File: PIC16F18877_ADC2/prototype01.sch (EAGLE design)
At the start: 34 parts, among them CN1 12V_IN, CN3 UART_IF, CN4 PIC_CN_H, CN5 AE-MICRO-SD-DIP, CN6 I2C_IF, SW1 10-XX, U1 XC6202P332TH, U2 PIC16F18877-I/P, U3 AE-AQM1602A, U4 AE-RTC-8564NB

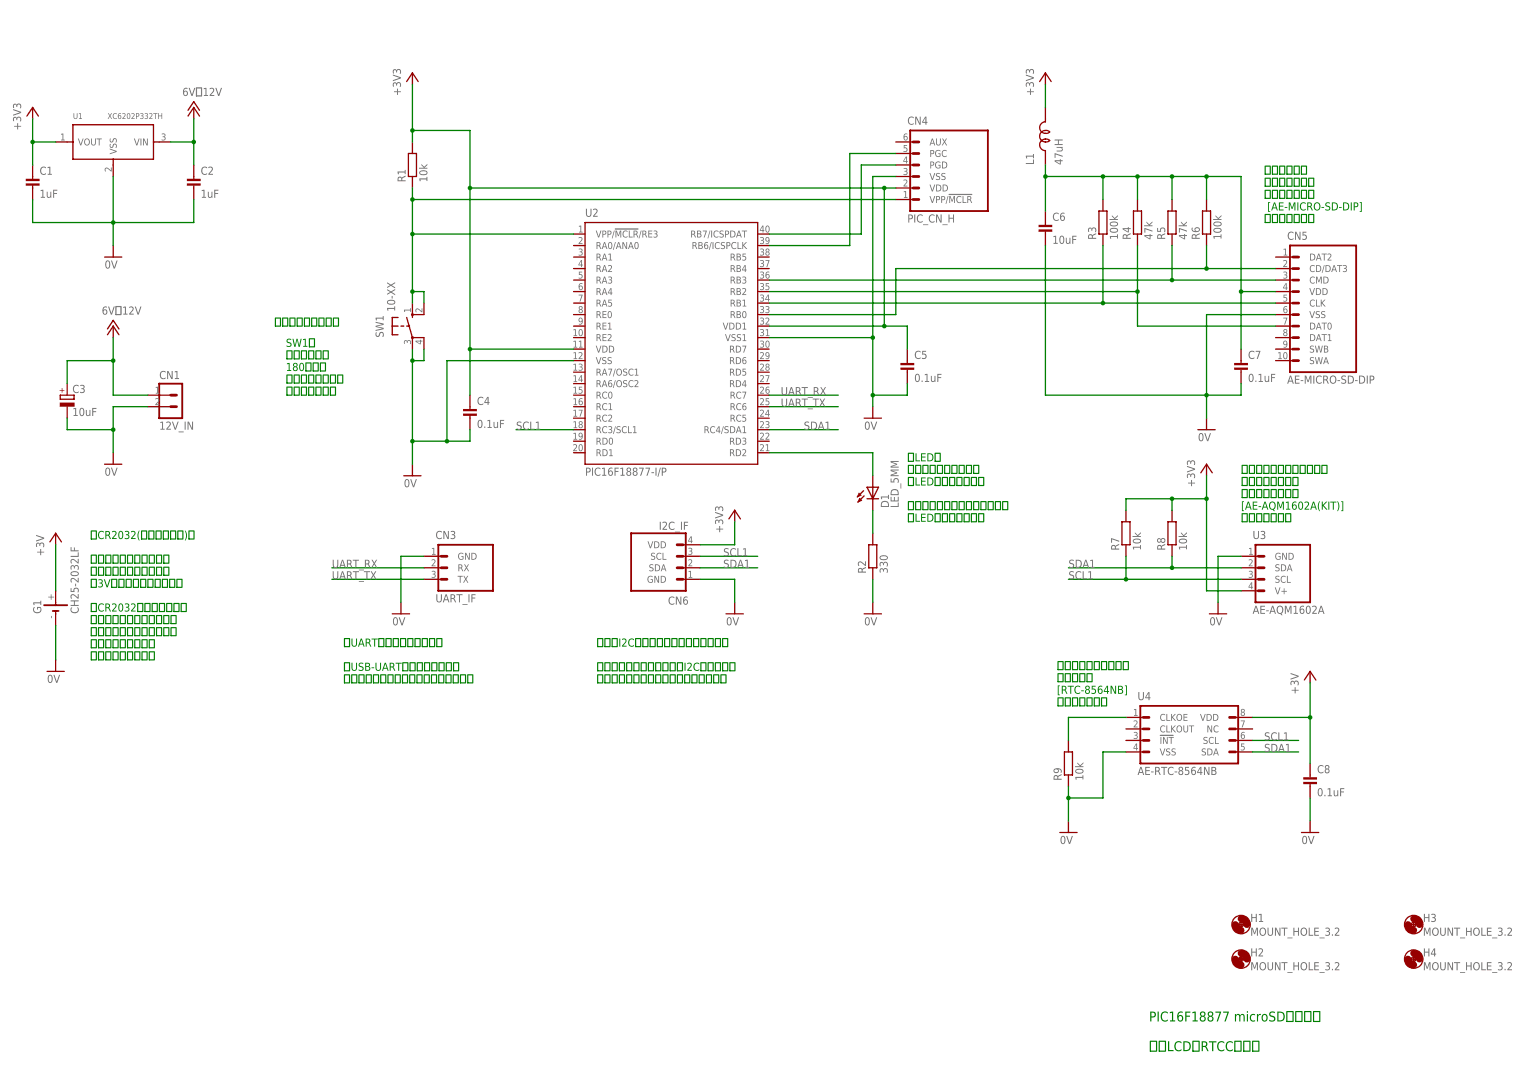
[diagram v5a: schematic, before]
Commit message: GPIO接続用コネクター増設
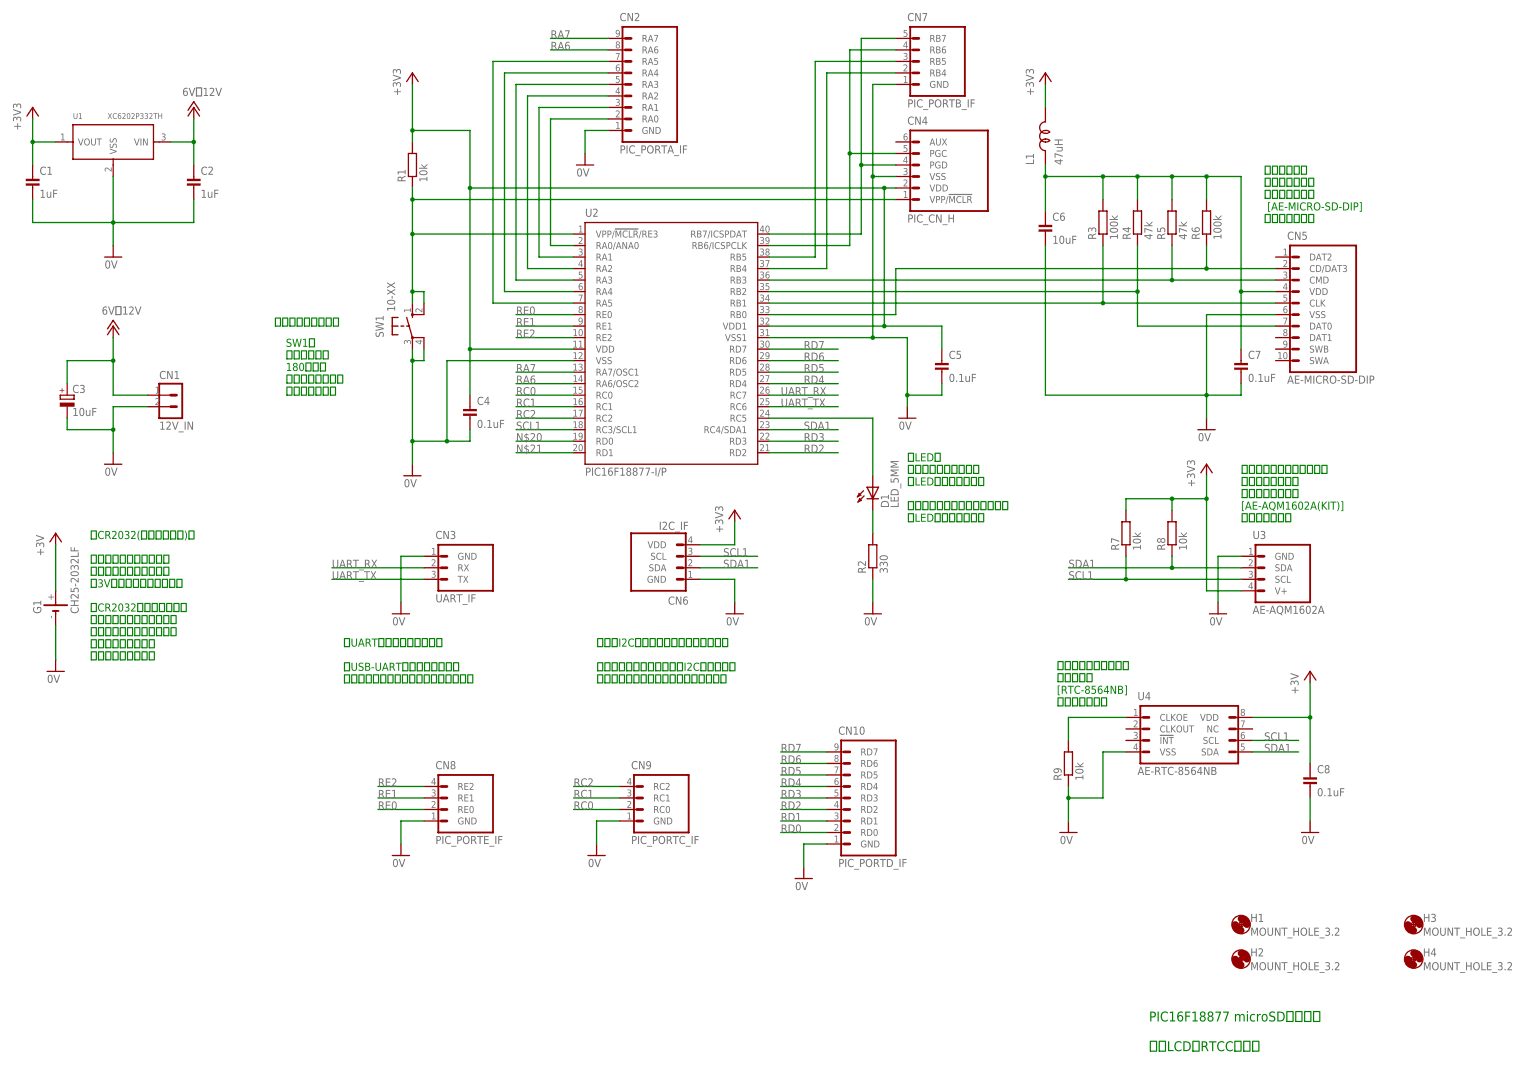
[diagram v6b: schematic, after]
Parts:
- added CN10: PIC_PORTD_IF, PartsForProto:PIC_PORTD_IF
- added CN2: PIC_PORTA_IF, PartsForProto:PIC_PORTA_IF
- added CN7: PIC_PORTB_IF, PartsForProto:PIC_PORTB_IF
- added CN8: PIC_PORTE_IF, PartsForProto:PIC_PORTE_IF
- added CN9: PIC_PORTC_IF, PartsForProto:PIC_PORTC_IF
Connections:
- new net N$10: CN2.RA0, U2.RA0/ANA0
- new net N$11: CN2.RA1, U2.RA1
- new net N$13: CN2.RA2, U2.RA2
- new net N$14: CN2.RA3, U2.RA3
- new net N$15: CN2.RA4, U2.RA4
- new net N$17: CN2.RA5, U2.RA5
- new net N$18: CN7.RB4, U2.RB4
- new net N$19: CN7.RB5, U2.RB5
- new net N$20: U2.RD0
- new net N$21: U2.RD1
- new net RA6: CN2.RA6, U2.RA6/OSC2
- new net RA7: CN2.RA7, U2.RA7/OSC1
- new net RC0: CN9.RC0, U2.RC0
- new net RC1: CN9.RC1, U2.RC1
- new net RC2: CN9.RC2, U2.RC2
- new net RD0: CN10.RD0
- new net RD1: CN10.RD1
- new net RD2: CN10.RD2, U2.RD2
- new net RD3: CN10.RD3, U2.RD3
- new net RD4: CN10.RD4, U2.RD4
- new net RD5: CN10.RD5, U2.RD5
- new net RD6: CN10.RD6, U2.RD6
- new net RD7: CN10.RD7, U2.RD7
- new net RE0: CN8.RE0, U2.RE0
- new net RE1: CN8.RE1, U2.RE1
- new net RE2: CN8.RE2, U2.RE2
- net 0V: now also CN10.GND, CN2.GND, CN7.GND, CN8.GND, CN9.GND
- net N$2: now also CN7.RB7
- net N$4: now also CN7.RB6
- net N$5: now also U2.RC5; no longer U2.RD2
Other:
- moved on the sheet: C5

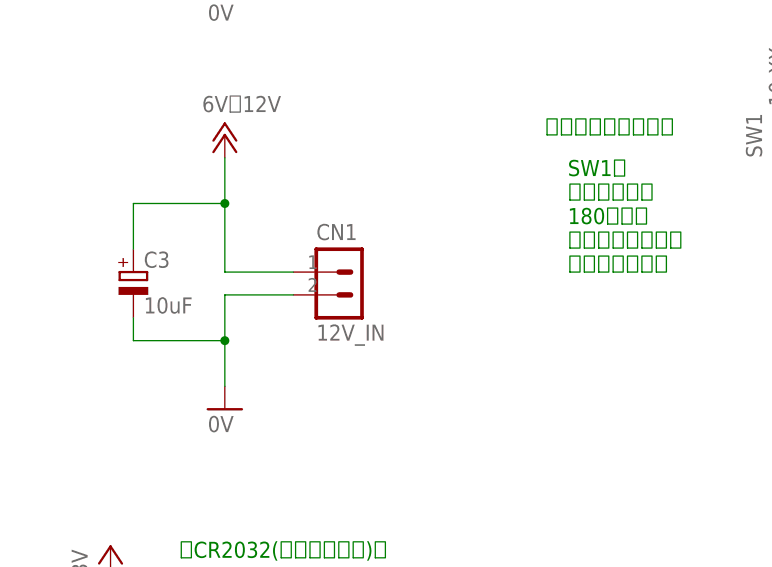
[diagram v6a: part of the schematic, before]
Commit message: 部品配置を修正
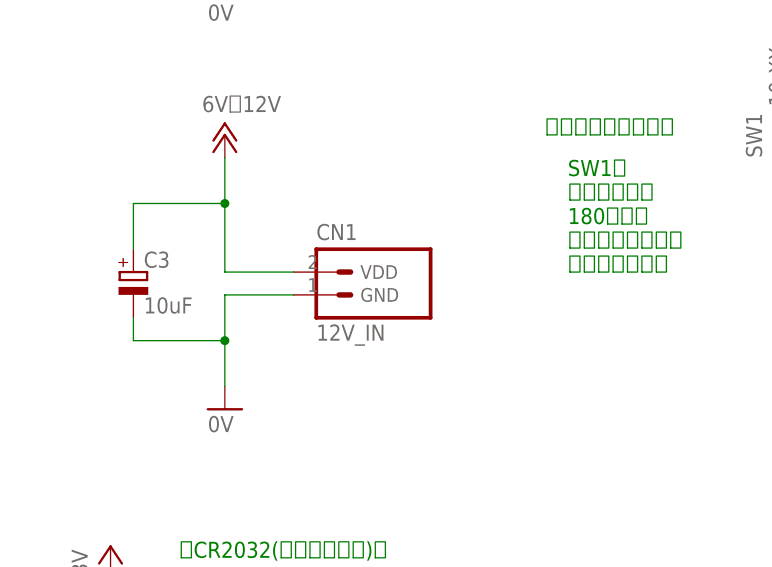
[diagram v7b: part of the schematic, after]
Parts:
- CN1: device Connectors:CONN_2PIN-L -> PartsForProto:POWER_IF
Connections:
- net +12V: now also CN1.VDD; no longer CN1.1
- net 0V: now also CN1.GND; no longer CN1.2
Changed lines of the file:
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@@
 <part name="GND10" library="Supply" deviceset="0V" device=""/>
 <part name="P+2" library="Supply" deviceset="+12V" device="" value="6V〜12V"/>
-<part name="CN1" library="Connectors" deviceset="CONN_2PIN" device="-L" value="12V_IN"/>
+<part name="CN1" library="PartsForProto" deviceset="POWER_IF" device="" value="12V_IN"/>
 <part name="+3V4" library="Supply" deviceset="+3V3" device=""/>
 <part name="U4" library="PartsForProto" deviceset="AE-RTC-8564NB" device=""/>
@@
 </segment>
 <segment>
-<pinref part="CN1" gate="G$1" pin="2"/>
+<pinref part="CN1" gate="G$1" pin="GND"/>
 <pinref part="GND10" gate="1" pin="0V"/>
 <wire x1="71.12" y1="152.4" x2="63.5" y2="152.4" width="0.1524" layer="91"/>
@@
 </segment>
 <segment>
-<pinref part="CN1" gate="G$1" pin="1"/>
+<pinref part="CN1" gate="G$1" pin="VDD"/>
 <pinref part="P+2" gate="1" pin="+12V"/>
 <wire x1="71.12" y1="154.94" x2="63.5" y2="154.94" width="0.1524" layer="91"/>
